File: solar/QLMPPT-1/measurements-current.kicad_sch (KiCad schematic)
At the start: 8 parts

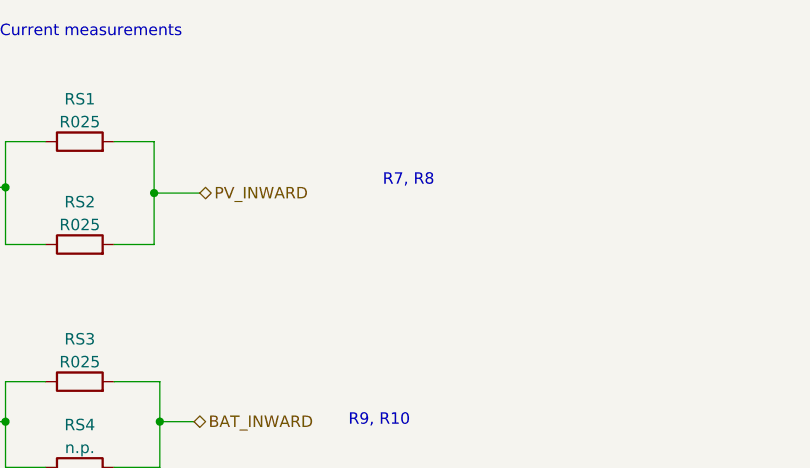
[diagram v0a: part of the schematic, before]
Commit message: Sketching boost converter
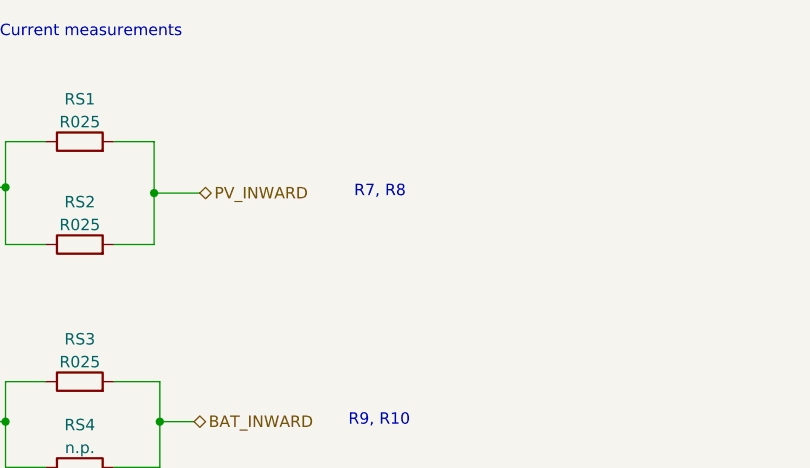
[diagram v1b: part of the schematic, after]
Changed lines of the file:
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@@
     (effects (font (size 1.27 1.27)) (justify left bottom))
   )
-  (text "R7, R8\n" (at 133.985 45.085 0)
+  (text "R7, R8\n" (at 130.81 46.355 0)
     (effects (font (size 1.27 1.27)) (justify left bottom))
   )
